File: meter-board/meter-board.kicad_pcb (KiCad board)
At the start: 4 copper layers, 100 x 50 mm, 291 parts, among them J1 2-1445053-2, J2 3-794636-8, J3 2-1445053-4, Q1 PMN100EPAX, Q2 2N7002K-AU_R1_000A2, U1 AP66300QFVBW-13, U10 TLV1814RTER, U11 TLV1814RTER, U12 TLV1814RTER, U13 TLV1814RTER, U14 TLV1814RTER, U15 TLV1814RTER, U16 TBD62183AFNG,EL, U17 TBD62183AFNG,EL, U18 TBD62183AFNG,EL, U19 TBD62183AFNG,EL, U2 TS431BIYLT, U20 TLV1814RTER, U21 SN74HC595BRWNR, U22 SN74HC595BRWNR, U23 SN74HC595BRWNR, U24 TBD62783AFNG,EL, U25 TBD62183AFNG,EL, U26 TBD62183AFNG,EL, U27 SN74LV4T125RGYR, U3 ACSC02-41SURKWA-F01, U4 ACSC02-41SURKWA-F01, U5 ACSC02-41SURKWA-F01, U6 157121S12700, U7 157121S12700, U8 157121S12700, U9 TLV1814RTER

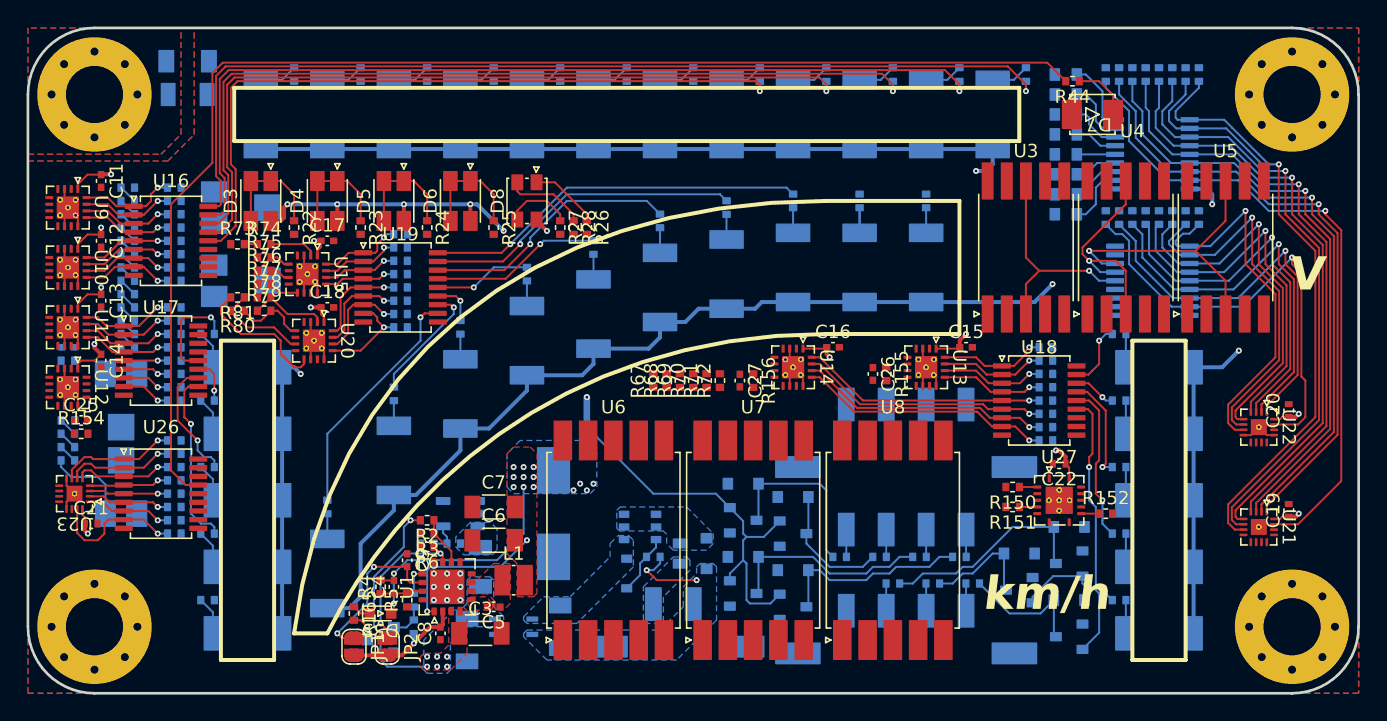
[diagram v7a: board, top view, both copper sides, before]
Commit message: update patterns
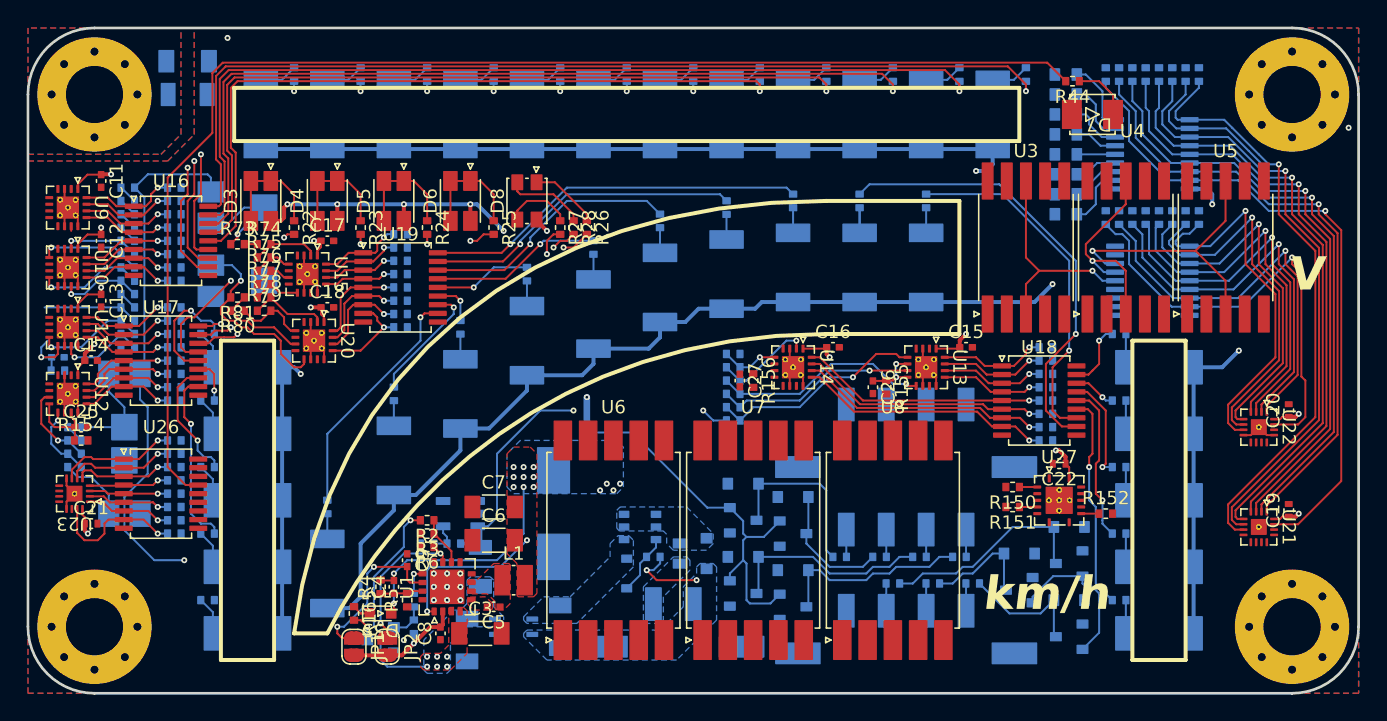
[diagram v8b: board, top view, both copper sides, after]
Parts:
- R67, R68, R69, R70, R71, R72: moved to B.Cu
- moved R67 6.71 mm to (53.0, 29.5), turned to 0 degrees
- moved R68 5.39 mm to (53.0, 28.5), turned to 0 degrees
- moved R69 4.12 mm to (53.0, 27.5), turned to 0 degrees
- moved R70 3.00 mm to (53.0, 26.5), turned to 0 degrees
- moved R71 2.24 mm to (53.0, 25.5), turned to 0 degrees
- moved R72 2.24 mm to (53.0, 24.5), turned to 0 degrees
- moved C24 1.06 mm to (2.25, 24.8)
- moved R153 1.06 mm to (2.25, 25.8)
- moved C26 1.00 mm to (63.5, 27.0)
- moved R155 1.00 mm to (64.5, 27.0)
- moved C14 0.75 mm to (4.75, 25.0), turned to 0 degrees
- moved R63 0.71 mm to (3.50, 30.0)
- moved R64 0.71 mm to (3.50, 31.0)
- moved R65 0.71 mm to (3.50, 32.0)
- moved R66 0.71 mm to (3.50, 33.0)
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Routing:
- net +5VREF: track 0.00 -> 120.2 mm, vias 0 -> 3
- net /G6R6_R1: track 0.00 -> 53.7 mm, vias 0 -> 2
- net /G6R6_G6: track 0.00 -> 49.6 mm, vias 0 -> 2
- net /G6R6_G5: track 0.00 -> 45.5 mm, vias 0 -> 2
- net /G6R6_G4: track 0.00 -> 42.9 mm, vias 0 -> 2
- net /G6R6_G3: track 0.00 -> 38.7 mm, vias 0 -> 2
- net /G6R6_G2: track 0.00 -> 34.2 mm, vias 0 -> 2
- net /R10_R9: track 0.00 -> 33.9 mm, vias 0 -> 1
- net /G6R6_G1: track 0.00 -> 29.1 mm, vias 0 -> 2
- net /R10_R10: track 0.00 -> 26.6 mm, vias 0 -> 1
- net Net-(U13D--): track 0.00 -> 16.3 mm, vias 0 -> 1
- net Net-(U13B--): track 0.00 -> 16.2 mm, vias 0 -> 1
- net Net-(U13C--): track 0.00 -> 15.2 mm, vias 0 -> 1
- net Net-(U14C--): track 0.00 -> 8.28 mm, vias 0 -> 1
- net Net-(U12A--): track 0.00 -> 7.73 mm
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- removed copper zone on B.Cu, net +5VREF
